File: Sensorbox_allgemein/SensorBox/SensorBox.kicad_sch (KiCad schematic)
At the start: 0 parts

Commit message: Update SensorBox.kicad_sch
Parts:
- added V1: 1, symbol Simulation_SPICE:VDC
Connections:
- new net GND_Box: V1.2
- new net VCC_Box: V1.1
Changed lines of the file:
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@@
 	(generator_version "8.0")
 	(paper "A4")
+	(global_label "VCC_Box"
+		(shape input)
+		(at 27.94 26.67 180)
+		(fields_autoplaced yes)
+		(effects
+			(font
+				(size 1.27 1.27)
+			)
+			(justify right)
+		)
+		(property "Intersheetrefs" "${INTERSHEET_REFS}"
+			(at 16.9115 26.67 0)
+			(effects
+				(font
+					(size 1.27 1.27)
+				)
+				(justify right)
+				(hide yes)
+			)
+		)
+	)
+	(global_label "GND_Box"
+		(shape input)
+		(at 27.94 36.83 180)
+		(fields_autoplaced yes)
+		(effects
+			(font
+				(size 1.27 1.27)
+			)
+			(justify right)
+		)
+		(property "Intersheetrefs" "${INTERSHEET_REFS}"
+			(at 16.6696 36.83 0)
+			(effects
+				(font
+					(size 1.27 1.27)
+				)
+				(justify right)
+				(hide yes)
+			)
+		)
+	)
+	(symbol
+		(lib_id "Simulation_SPICE:VDC")
+		(at 27.94 31.75 0)
+		(unit 1)
+		(exclude_from_sim no)
+		(in_bom yes)
+		(on_board yes)
+		(dnp no)
+		(fields_autoplaced yes)
+		(property "Reference" "V1"
+			(at 31.75 30.3501 0)
+			(effects
+				(font
+					(size 1.27 1.27)
+				)
+				(justify left)
+			)
+		)
+		(property "Value" "1"
+			(at 31.75 32.8901 0)
+			(effects
+				(font
+					(size 1.27 1.27)
+				)
+				(justify left)
+			)
+		)
+		(property "Footprint" ""
+			(at 27.94 31.75 0)
+			(effects
+				(font
+					(size 1.27 1.27)
+				)
+				(hide yes)
+			)
+		)
+		(property "Datasheet" "https://ngspice.sourceforge.io/docs/ngspice-html-manual/manual.xhtml#sec_Independent_Sources_for"
+			(at 27.94 31.75 0)
+			(effects
+				(font
+					(size 1.27 1.27)
+				)
+				(hide yes)
+			)
+		)
+		(property "Description" "Voltage source, DC"
+			(at 27.94 31.75 0)
+			(effects
+				(font
+					(size 1.27 1.27)
+				)
+				(hide yes)
+			)
+		)
+		(property "Sim.Pins" "1=+ 2=-"
+			(at 27.94 31.75 0)
+			(effects
+				(font
+					(size 1.27 1.27)
+				)
+				(hide yes)
+			)
+		)
+		(property "Sim.Type" "DC"
+			(at 27.94 31.75 0)
+			(effects
+				(font
+					(size 1.27 1.27)
+				)
+				(hide yes)
+			)
+		)
+		(property "Sim.Device" "V"
+			(at 27.94 31.75 0)
+			(effects
+				(font
+					(size 1.27 1.27)
+				)
+				(justify left)
+				(hide yes)
+			)
+		)
+		(pin "2"
+		)
+		(pin "1"
+		)
+		(instances
+			(project "SensorBox"
+				(path "/7cbe8151-7294-42e6-9c4e-6ec8952d674f"
+					(reference "V1")
+					(unit 1)
+				)
+			)
+		)
+	)
 	(sheet_instances
 		(path "/"

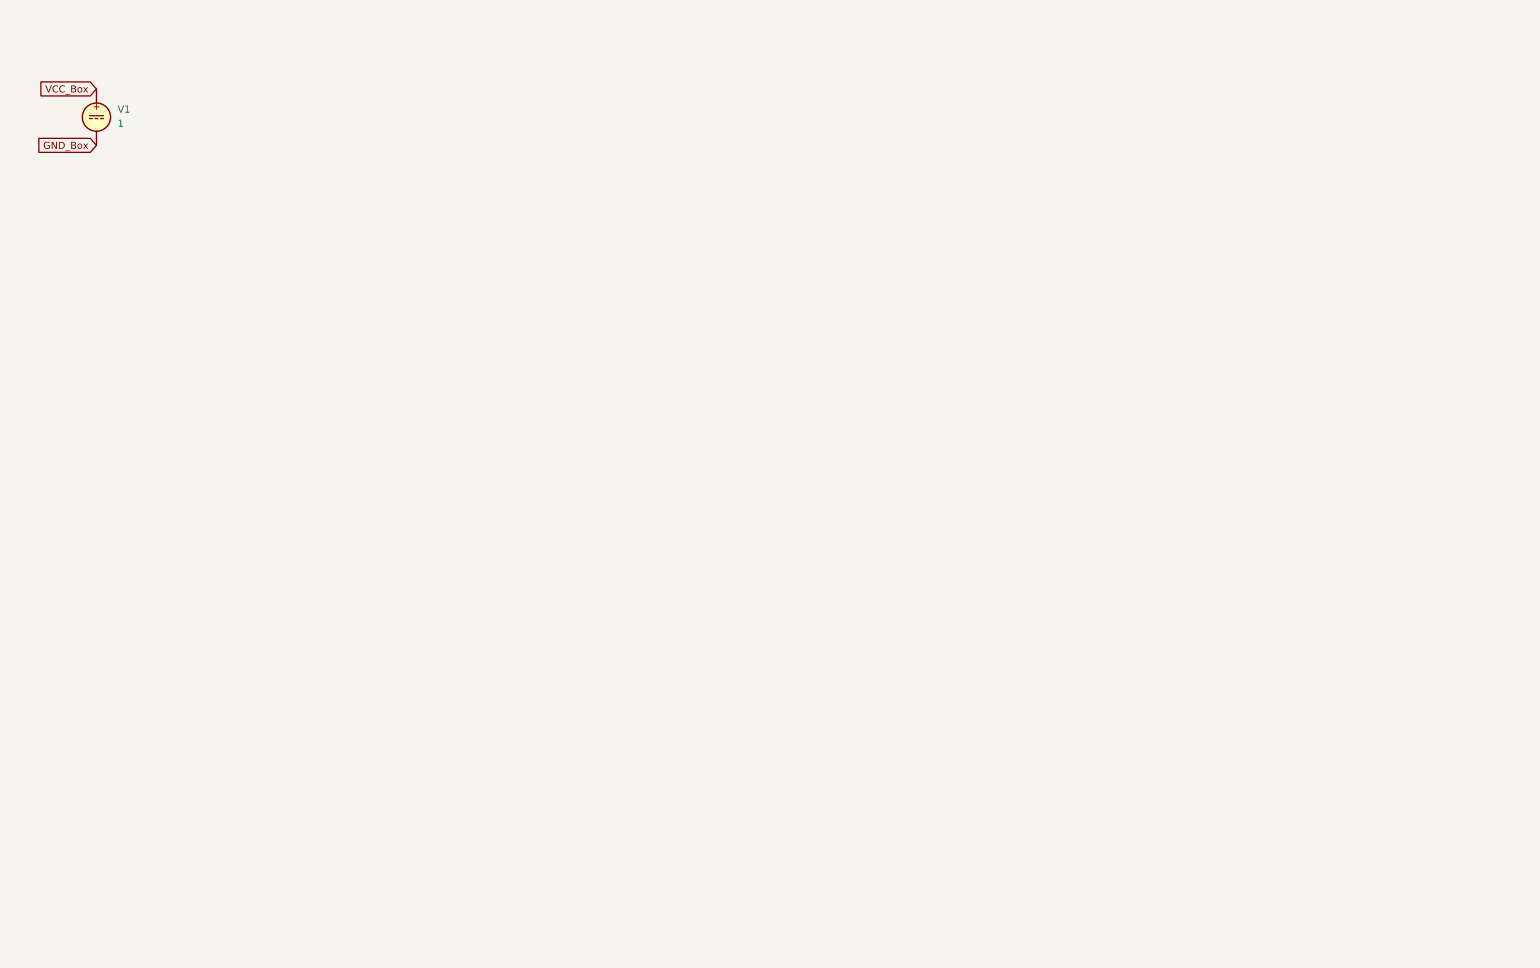
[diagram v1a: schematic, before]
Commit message: Hauptschaltung
Sensorbox, erste Hauptschaltung realisiert --> ESP32 C6 selbst designt und eingebaut und die restlichen Funktionen eingebaut --> SD Karte mit ESP verbunden, Spannungsregler eingebaut für die Spannung vom ESP

Co-Authored-By: LinusMarte <174097811+LinusMarte@users.noreply.github.com>
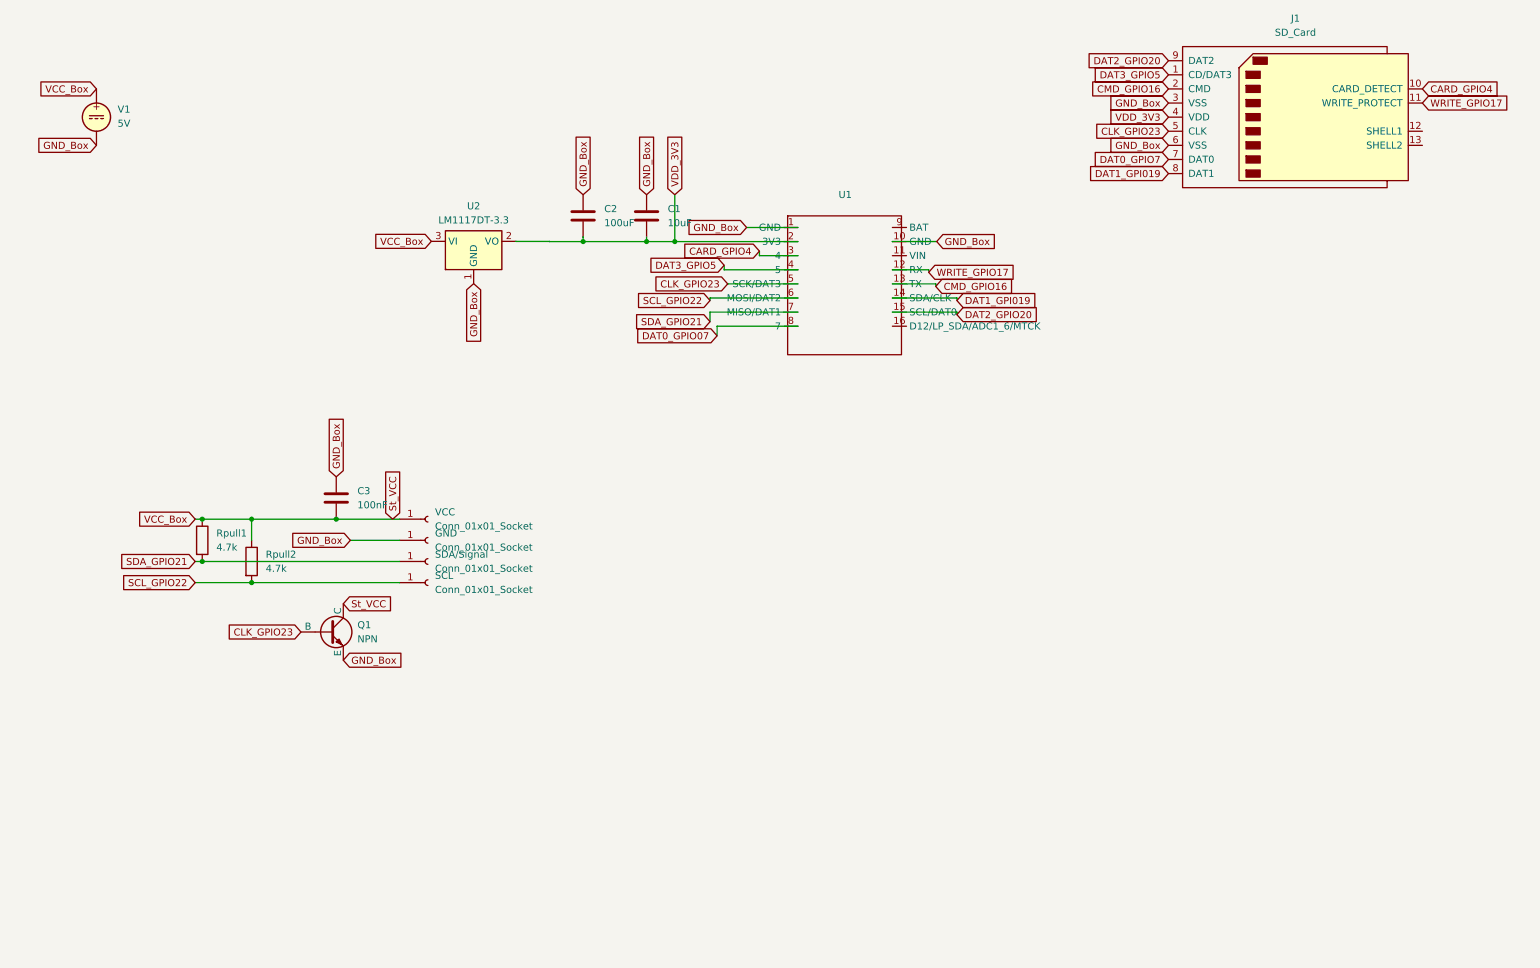
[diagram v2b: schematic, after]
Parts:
- added C1: 10uF, Capacitor_SMD:C_0402_1005Metric_Pad0.74x0.62mm_HandSolder, symbol Device:C
- added C2: 100uF, Capacitor_SMD:C_0402_1005Metric_Pad0.74x0.62mm_HandSolder, symbol Device:C
- added C3: 100nF, Capacitor_SMD:C_0402_1005Metric_Pad0.74x0.62mm_HandSolder, symbol Device:C
- added GND, SCL, SDA/Signal, VCC: Conn_01x01_Socket, Connector_PinHeader_2.00mm:PinHeader_1x01_P2.00mm_Vertical, symbol Connector:Conn_01x01_Socket
- added J1: SD_Card, symbol Connector:SD_Card
- added Q1: NPN, symbol Simulation_SPICE:NPN
- added Rpull1, Rpull2: 4.7k, Resistor_SMD:R_0402_1005Metric, symbol Device:R
- added U1: ~, ESP32_C6:ESP32_C6_BEETLE, symbol ESP32_C6_KIT:ESP32_C6_Beetle
- added U2: LM1117DT-3.3, Package_TO_SOT_SMD:TO-252-3_TabPin2, symbol Regulator_Linear:LM1117DT-3.3
- V1: value 1 -> 5V
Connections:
- net GND_Box: now also C1.2, C2.2, C3.2, GND.1 (Pin_1), J1.3 (VSS), J1.6 (VSS), Q1.3 (E), U1.1 (GND), U1.10 (GND), U2.1 (GND)
- net VCC_Box renamed St_VCC
- net St_VCC: now also C3.1, Q1.1 (C), Rpull1.1, Rpull2.1, U2.3 (VI), VCC.1 (Pin_1)
- new net CARD_GPIO4: J1.10 (CARD_DETECT), U1.3 (4)
- new net CLK_GPIO23: J1.5 (CLK), Q1.2 (B), U1.5 (SCK/DAT3)
- new net CMD_GPIO16: J1.2 (CMD), U1.13 (TX)
- new net DAT0_GPIO07: U1.8 (7)
- new net DAT0_GPIO7: J1.7 (DAT0)
- new net DAT1_GPI019: J1.8 (DAT1), U1.14 (SDA/CLK)
- new net DAT2_GPIO20: J1.9 (DAT2), U1.15 (SCL/DAT0)
- new net DAT3_GPIO5: J1.1 (CD/DAT3), U1.4 (5)
- new net SCL_GPIO22: Rpull2.2, SCL.1 (Pin_1), U1.6 (MOSI/DAT2)
- new net SDA_GPIO21: Rpull1.2, SDA/Signal.1 (Pin_1), U1.7 (MISO/DAT1)
- new net VDD_3V3: C1.1, C2.1, J1.4 (VDD), U1.2 (3V3), U2.2 (VO)
- new net WRITE_GPIO17: J1.11 (WRITE_PROTECT), U1.12 (RX)

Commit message: Main Sensor-Schaltung Revision 2
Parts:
- removed GND: Conn_01x01_Socket, Connector_PinHeader_2.00mm:PinHeader_1x01_P2.00mm_Vertical, symbol Connector:Conn_01x01_Socket
- removed U1: ~, ESP32_C6:ESP32_C6_BEETLE, symbol ESP32_C6_KIT:ESP32_C6_Beetle
- removed U2: LM1117DT-3.3, Package_TO_SOT_SMD:TO-252-3_TabPin2, symbol Regulator_Linear:LM1117DT-3.3
- removed V1: 5V, symbol Simulation_SPICE:VDC
- added Cin: 680µF, Capacitor_SMD:C_0402_1005Metric_Pad0.74x0.62mm_HandSolder, symbol Device:C
- added Cout: 220µF, Capacitor_SMD:C_0402_1005Metric_Pad0.74x0.62mm_HandSolder, symbol Device:C
- added D1: 1N5824, 1N5824:DIOAD1898W129L762D1143, symbol 1N5824:1N5824
- added D3: LED, LED_SMD:LED_0402_1005Metric, symbol Device:LED
- added GND1: Conn_01x01_Socket, Connector_PinHeader_2.00mm:PinHeader_1x01_P2.00mm_Vertical, symbol Connector:Conn_01x01_Socket
- added HM2: BME280, BME280_foot:BME280, symbol BME280_sym:BME280
- added L1: 33µH, Inductor_SMD:L_0402_1005Metric_Pad0.77x0.64mm_HandSolder, symbol Device:L
- added R1, R2: 4.7k, Resistor_SMD:R_0402_1005Metric, symbol Device:R
- added Rvor: 330R, Resistor_SMD:R_0402_1005Metric, symbol Device:R
- added Rwid: 1k, Resistor_SMD:R_0402_1005Metric, symbol Device:R
- added U1: LM2596S-3.3, Package_TO_SOT_SMD:TO-263-5_TabPin3, symbol Regulator_Switching:LM2596S-3.3
- added U2: PS1-O3-100, PS1O3100, symbol PS1-O3-100:PS1-O3-100
- added U3: Beetle ESP32-C6, ESP32_C6_Firma:Beetle ESP32-C6, symbol beetle_esp32-c6:Beetle_ESP32-C6
- added U4: ~, Battery_6V:Bat_6V, symbol 6V_Battery_SensorBox:Battery_6V
- added U5: HPP845E131R5, SON6_HPP845E131R5_TEC, symbol HPP845E131R5:HPP845E131R5
- C1: value 10uF -> 0.1uF
- C2: value 100uF -> 0.1uF
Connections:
- net CARD_GPIO4: now also U3.3 (GPIO4)
- net CLK_GPIO23: now also Rwid.2, U3.5 (GPIO23); no longer Q1.2 (B)
- net CMD_GPIO16: now also U3.12 (GPIO16)
- net DAT0_GPIO07: now also U3.8 (GPIO7)
- net DAT3_GPIO5: now also U3.4 (GPIO5)
- net SCL_GPIO22: now also U3.6 (GPIO22)
- net SDA_GPIO21: now also U3.7 (GPIO21)
- net VDD_3V3: now also Cout.1, L1.2, U1.4 (FB), U3.2 (3V3); no longer C1.1, C2.1
- net DAT1_GPI019: no longer names the net of J1.8 (DAT1)
- net DAT2_GPIO20: no longer names the net of J1.9 (DAT2)
- net GND_Box renamed GND1
- net GND1: now also Cin.2, Cout.2, D1.A, D3.1 (K), GND1.1 (Pin_1), HM2.1 (GND_1), HM2.5 (SDO), HM2.7 (GND_2), U1.3 (GND), U1.5 (~{ON}/OFF), U3.1 (GND), U3.15 (GND), U4.2 (V-)
- net St_VCC renamed Steuerung_VCC
- net Steuerung_VCC: now also Cin.1, U1.1 (VIN), U4.1 (V+); no longer Q1.1 (C)
- net WRITE_GPIO17: no longer names the net of J1.11 (WRITE_PROTECT)
- new net: D3.2 (A), Rvor.1
- new net: Rvor.2, U3.9 (GPIO6)
- new net: D1.C, L1.1, U1.2 (OUT)
- new net: Q1.2 (B), Rwid.1
- new net SCK_1: HM2.4 (SCK), R1.1
- new net SDA_1: HM2.3 (SDI), R2.1
- new net Steurung_VCC: Q1.1 (C)
- new net V+: C1.1, C2.1, HM2.2 (CSB), HM2.6 (VDDIO), HM2.8 (VDD), R1.2, R2.2
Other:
- note added: "9V Batterie"
- note added: "ESP32-C6"
- note added: "Memory-Card"
- note added: "Spannungsregler-3.3V"
- note added: "Steckpins für den externen Sensor"
- moved on the sheet: J1, Q1, Rpull1, Rpull2, SCL, SDA/Signal, VCC

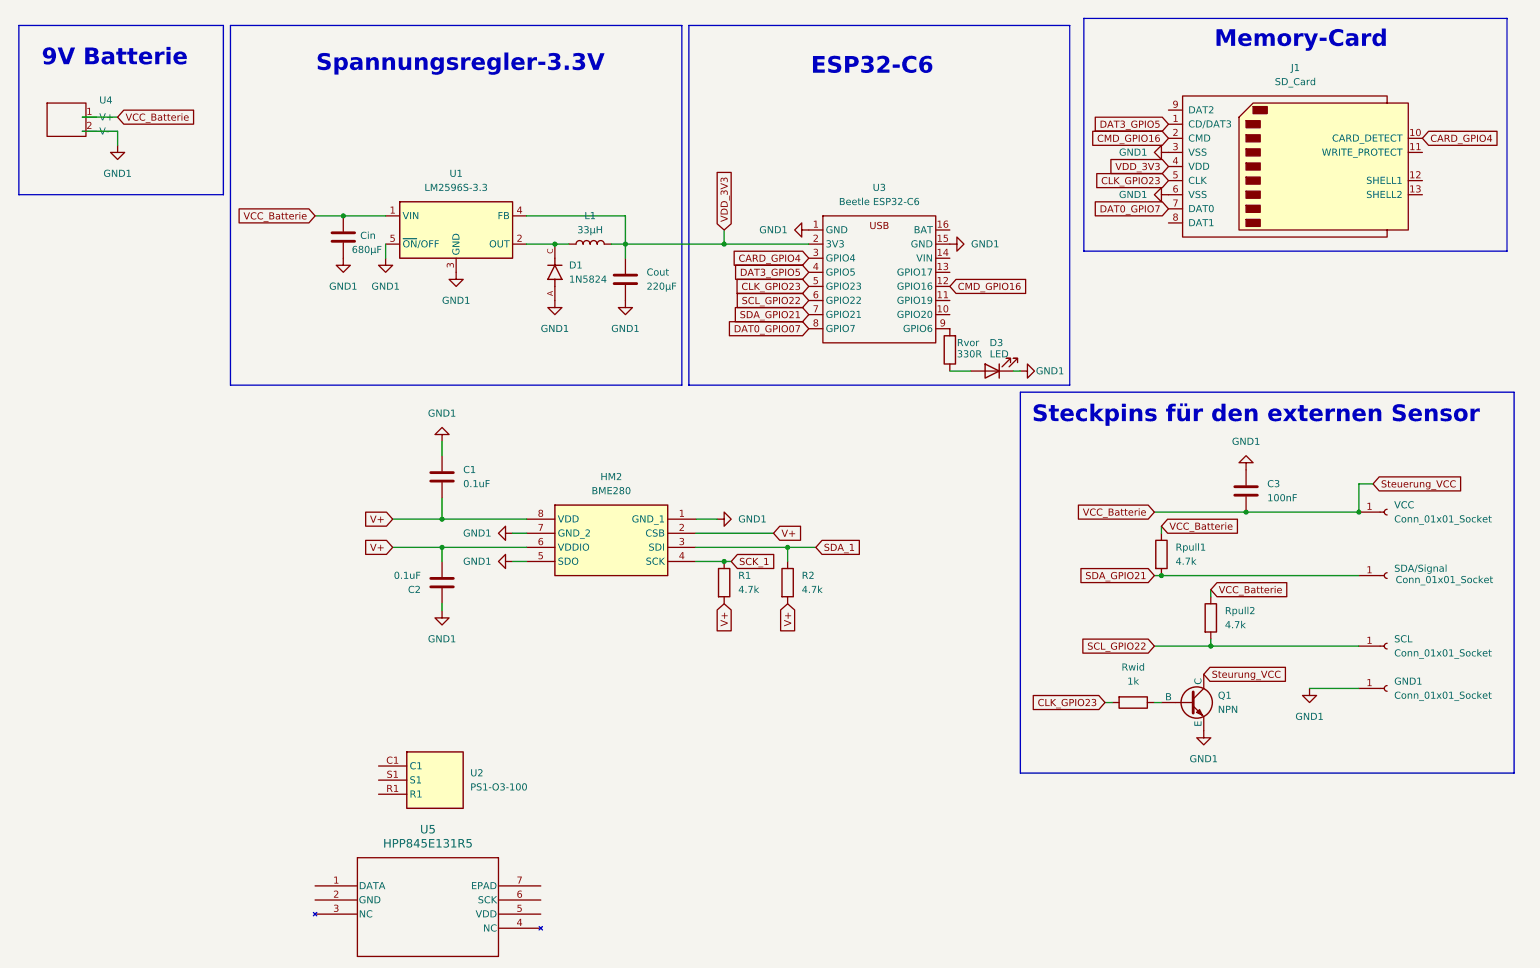
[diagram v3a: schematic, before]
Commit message: Änderung_schematic
Luftfeuchtigkeitssensor bearbeitet
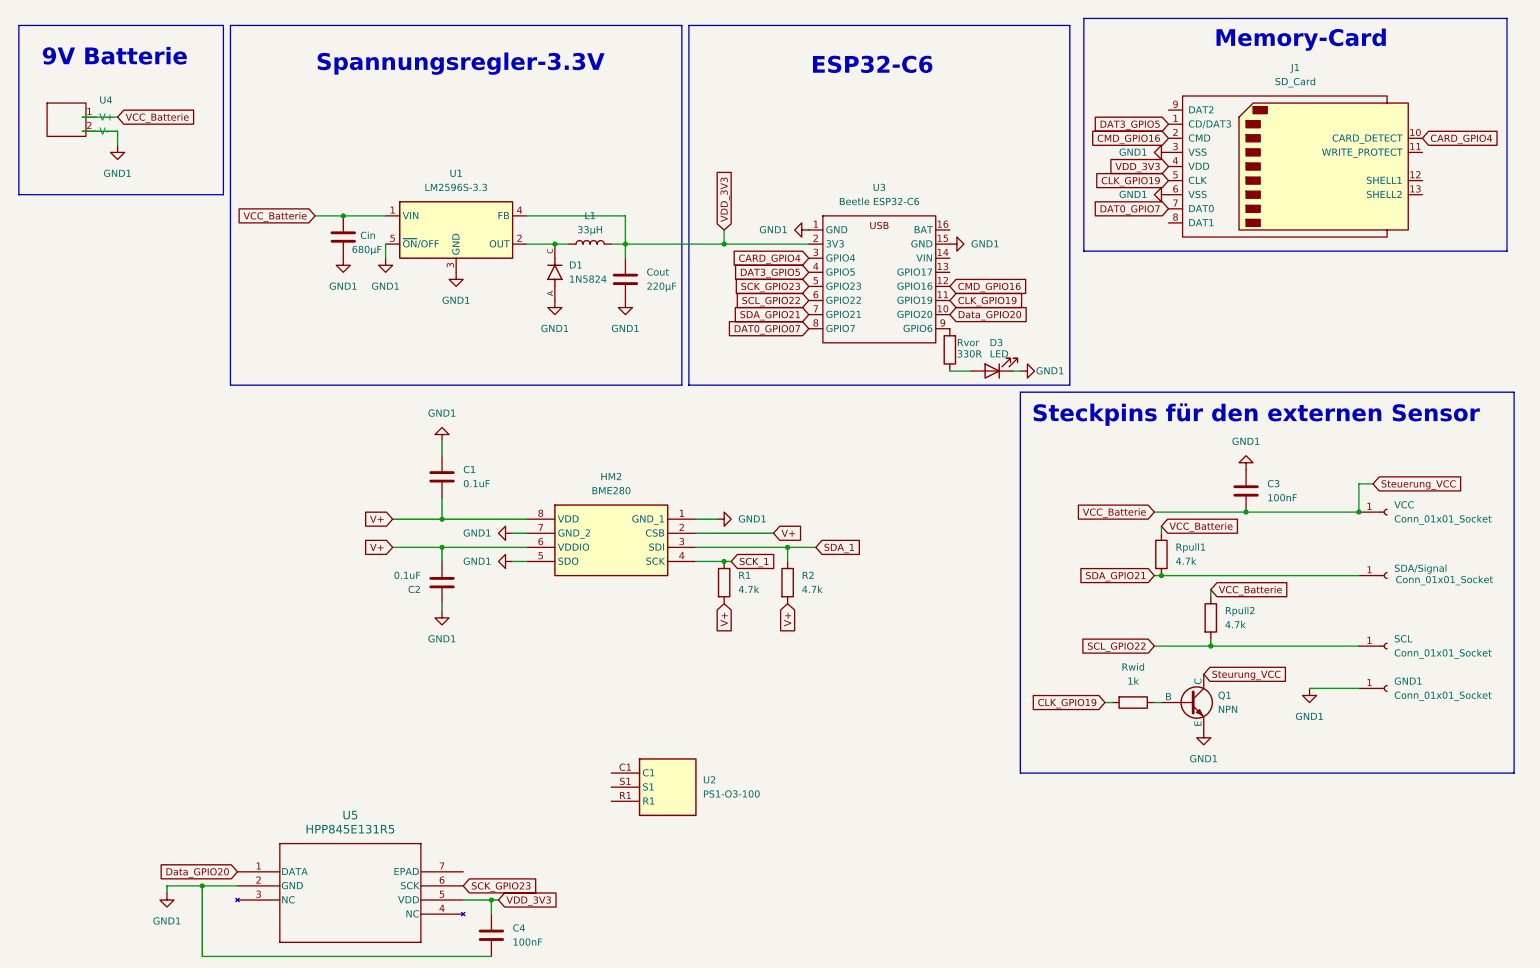
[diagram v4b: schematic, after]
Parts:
- added C4: 100nF, Capacitor_SMD:C_0402_1005Metric_Pad0.74x0.62mm_HandSolder, symbol Device:C
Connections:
- net GND1: now also U5.2 (GND), C4.2
- net VDD_3V3: now also U5.5 (VDD), C4.1
- net Data_GPIO20: now reaches U3.10 (GPIO20)
- net Data_GPIO20: now also U5.1 (DATA)
- net CLK_GPIO19: now reaches U3.11 (GPIO19)
- net CLK_GPIO19: now also J1.5 (CLK), Rwid.2
- net SCK_GPIO23: now reaches U5.6 (SCK)
- net SCK_GPIO23: now also U3.5 (GPIO23)
- removed net CLK_GPIO23: J1.5 (CLK), Rwid.2, U3.5 (GPIO23)
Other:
- moved on the sheet: U2, U5
